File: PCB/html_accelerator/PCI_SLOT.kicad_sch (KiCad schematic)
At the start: 13 parts, among them J2 Bus_PCI_Express_x8, J3 PCIexpress_bracket, U1 MCS9990

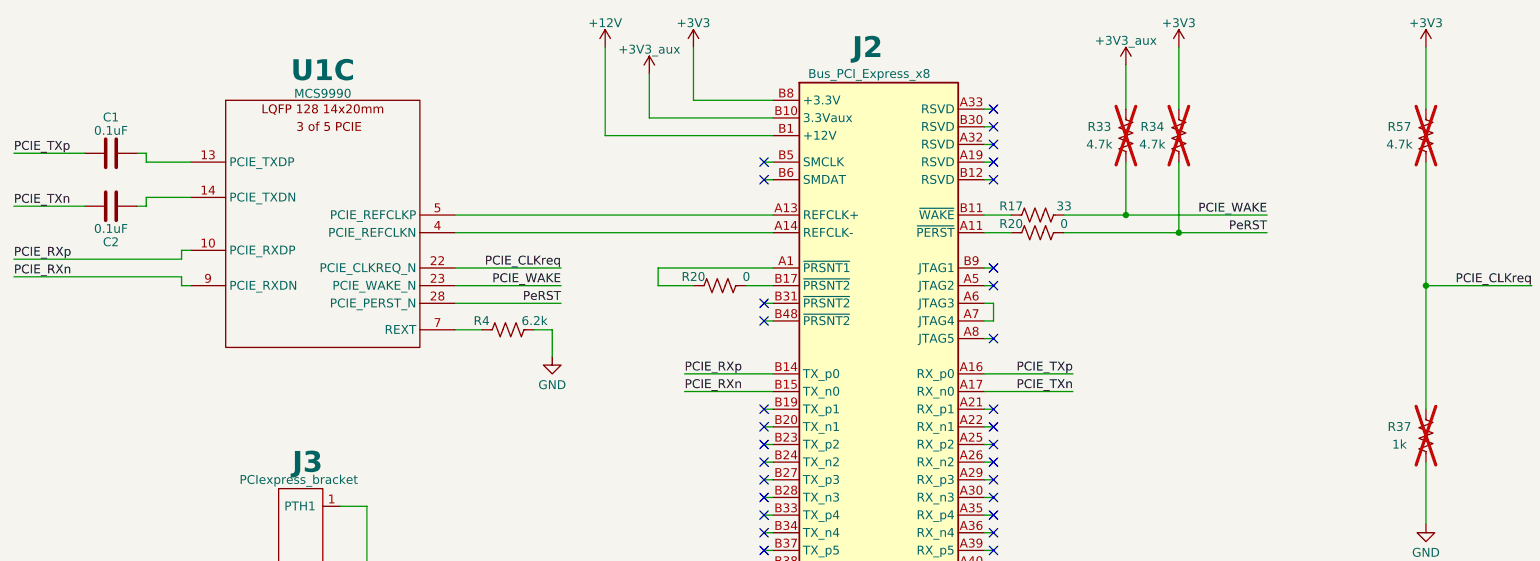
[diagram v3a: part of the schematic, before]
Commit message: EMMC symbols and netlist
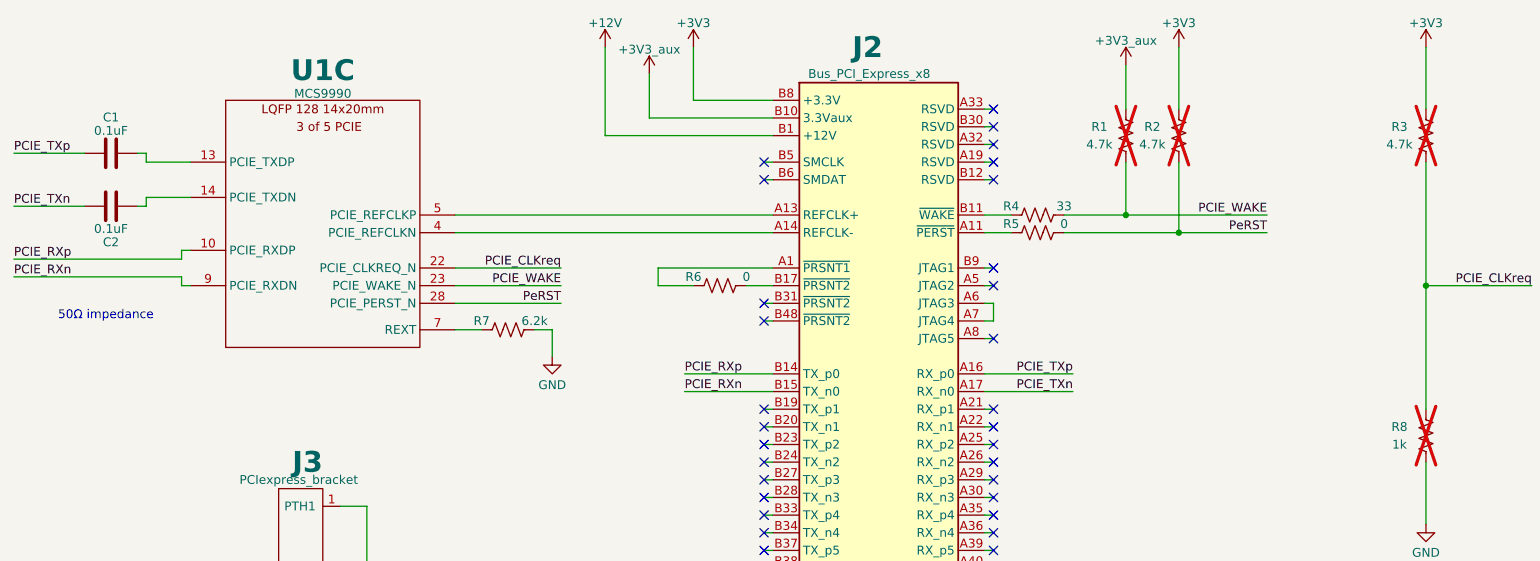
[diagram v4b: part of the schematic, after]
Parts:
- renumbered R33 to R1, R34 to R2, R57 to R3, R17 to R4, R20 to R5, R20 to R6, R4 to R7, R37 to R8
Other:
- note added: "50Ω impedance"
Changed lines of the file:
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@@
     (stroke (width 0) (type default))
+  )
+  (text "50Ω impedance" (at 34.29 95.25 0)
+    (effects (font (size 1.27 1.27)) (justify left bottom))
   )
   (label "PCIE_RXp" (at 124.46 102.87 0) (fields_autoplaced)
@@
   (symbol (lib_id "Device:R_US") (at 129.54 90.17 90) (unit 1)
     (in_bom yes) (on_board yes) (dnp no)
-    (property "Reference" "R20" (at 125.73 88.9 90)
+    (property "Reference" "R6" (at 125.73 88.9 90)
       (effects (font (size 1.27 1.27)))
     )
@@
       (project "html_accelerator"
         (path "/12b3a7c9-141f-40ba-9ebb-094b58bfa6c7/3421334e-11b3-46c8-b0f2-353f0fa6f362"
-          (reference "R20") (unit 1)
+          (reference "R6") (unit 1)
         )
       )
@@
   (symbol (lib_id "power:GND") (at 231.14 124.46 0) (unit 1)
     (in_bom yes) (on_board yes) (dnp no) (fields_autoplaced)
-    (property "Reference" "#PWR010" (at 231.14 130.81 0)
+    (property "Reference" "#PWR08" (at 231.14 130.81 0)
       (effects (font (size 1.27 1.27)) hide)
     )
@@
       (project "html_accelerator"
         (path "/12b3a7c9-141f-40ba-9ebb-094b58bfa6c7/3421334e-11b3-46c8-b0f2-353f0fa6f362"
-          (reference "#PWR010") (unit 1)
+          (reference "#PWR08") (unit 1)
         )
       )
@@
   (symbol (lib_id "power:+3V3") (at 119.38 59.69 0) (unit 1)
     (in_bom yes) (on_board yes) (dnp no)
-    (property "Reference" "#PWR07" (at 119.38 63.5 0)
+    (property "Reference" "#PWR06" (at 119.38 63.5 0)
       (effects (font (size 1.27 1.27)) hide)
     )
@@
       (project "html_accelerator"
         (path "/12b3a7c9-141f-40ba-9ebb-094b58bfa6c7/3421334e-11b3-46c8-b0f2-353f0fa6f362"
-          (reference "#PWR07") (unit 1)
+          (reference "#PWR06") (unit 1)
         )
       )
@@
   (symbol (lib_id "Device:R_US") (at 187.96 68.58 180) (unit 1)
     (in_bom yes) (on_board yes) (dnp yes)
-    (property "Reference" "R33" (at 184.15 67.31 0)
+    (property "Reference" "R1" (at 184.15 67.31 0)
       (effects (font (size 1.27 1.27)))
     )
@@
       (project "html_accelerator"
         (path "/12b3a7c9-141f-40ba-9ebb-094b58bfa6c7/3421334e-11b3-46c8-b0f2-353f0fa6f362"
-          (reference "R33") (unit 1)
+          (reference "R1") (unit 1)
         )
       )
@@
   (symbol (lib_id "power:GND") (at 78.74 140.97 0) (unit 1)
     (in_bom yes) (on_board yes) (dnp no) (fields_autoplaced)
-    (property "Reference" "#PWR01" (at 78.74 147.32 0)
+    (property "Reference" "#PWR09" (at 78.74 147.32 0)
       (effects (font (size 1.27 1.27)) hide)
     )
@@
       (project "html_accelerator"
         (path "/12b3a7c9-141f-40ba-9ebb-094b58bfa6c7/3421334e-11b3-46c8-b0f2-353f0fa6f362"
-          (reference "#PWR01") (unit 1)
+          (reference "#PWR09") (unit 1)
         )
       )
@@
         )
         (path "/12b3a7c9-141f-40ba-9ebb-094b58bfa6c7/3421334e-11b3-46c8-b0f2-353f0fa6f362"
-          (reference "J1") (unit 1)
+          (reference "J2") (unit 1)
         )
       )
@@
   (symbol (lib_id "power:+12V") (at 113.03 55.88 0) (unit 1)
     (in_bom yes) (on_board yes) (dnp no) (fields_autoplaced)
-    (property "Reference" "#PWR04" (at 113.03 59.69 0)
+    (property "Reference" "#PWR01" (at 113.03 59.69 0)
       (effects (font (size 1.27 1.27)) hide)
     )
@@
       (project "html_accelerator"
         (path "/12b3a7c9-141f-40ba-9ebb-094b58bfa6c7/3421334e-11b3-46c8-b0f2-353f0fa6f362"
-          (reference "#PWR04") (unit 1)
+          (reference "#PWR01") (unit 1)
         )
       )
@@
   (symbol (lib_id "power:+3V3") (at 125.73 55.88 0) (unit 1)
     (in_bom yes) (on_board yes) (dnp no) (fields_autoplaced)
-    (property "Reference" "#PWR03" (at 125.73 59.69 0)
+    (property "Reference" "#PWR02" (at 125.73 59.69 0)
       (effects (font (size 1.27 1.27)) hide)
     )
@@
       (project "html_accelerator"
         (path "/12b3a7c9-141f-40ba-9ebb-094b58bfa6c7/3421334e-11b3-46c8-b0f2-353f0fa6f362"
-          (reference "#PWR03") (unit 1)
+          (reference "#PWR02") (unit 1)
         )
       )
@@
   (symbol (lib_id "power:GND") (at 152.4 151.13 0) (unit 1)
     (in_bom yes) (on_board yes) (dnp no) (fields_autoplaced)
-    (property "Reference" "#PWR02" (at 152.4 157.48 0)
+    (property "Reference" "#PWR010" (at 152.4 157.48 0)
       (effects (font (size 1.27 1.27)) hide)
     )
@@
       (project "html_accelerator"
         (path "/12b3a7c9-141f-40ba-9ebb-094b58bfa6c7/3421334e-11b3-46c8-b0f2-353f0fa6f362"
-          (reference "#PWR02") (unit 1)
+          (reference "#PWR010") (unit 1)
         )
       )
@@
   (symbol (lib_id "Device:R_US") (at 99.06 96.52 90) (unit 1)
     (in_bom yes) (on_board yes) (dnp no)
-    (property "Reference" "R4" (at 95.25 95.25 90)
+    (property "Reference" "R7" (at 95.25 95.25 90)
       (effects (font (size 1.27 1.27)))
     )
@@
       (project "html_accelerator"
         (path "/12b3a7c9-141f-40ba-9ebb-094b58bfa6c7/3421334e-11b3-46c8-b0f2-353f0fa6f362"
-          (reference "R4") (unit 1)
+          (reference "R7") (unit 1)
         )
       )
@@
   (symbol (lib_id "Device:R_US") (at 175.26 82.55 90) (unit 1)
     (in_bom yes) (on_board yes) (dnp no)
-    (property "Reference" "R20" (at 171.45 81.28 90)
+    (property "Reference" "R5" (at 171.45 81.28 90)
       (effects (font (size 1.27 1.27)))
     )
@@
       (project "html_accelerator"
         (path "/12b3a7c9-141f-40ba-9ebb-094b58bfa6c7/3421334e-11b3-46c8-b0f2-353f0fa6f362"
-          (reference "R20") (unit 1)
+          (reference "R5") (unit 1)
         )
       )
@@
   (symbol (lib_id "power:+3V3") (at 231.14 55.88 0) (unit 1)
     (in_bom yes) (on_board yes) (dnp no) (fields_autoplaced)
-    (property "Reference" "#PWR09" (at 231.14 59.69 0)
+    (property "Reference" "#PWR04" (at 231.14 59.69 0)
       (effects (font (size 1.27 1.27)) hide)
     )
@@
       (project "html_accelerator"
         (path "/12b3a7c9-141f-40ba-9ebb-094b58bfa6c7/3421334e-11b3-46c8-b0f2-353f0fa6f362"
-          (reference "#PWR09") (unit 1)
+          (reference "#PWR04") (unit 1)
         )
       )
@@
   (symbol (lib_id "Device:R_US") (at 231.14 68.58 180) (unit 1)
     (in_bom yes) (on_board yes) (dnp yes)
-    (property "Reference" "R57" (at 227.33 67.31 0)
+    (property "Reference" "R3" (at 227.33 67.31 0)
       (effects (font (size 1.27 1.27)))
     )
@@
       (project "html_accelerator"
         (path "/12b3a7c9-141f-40ba-9ebb-094b58bfa6c7/3421334e-11b3-46c8-b0f2-353f0fa6f362"
-          (reference "R57") (unit 1)
+          (reference "R3") (unit 1)
         )
       )
@@
   (symbol (lib_id "Device:R_US") (at 175.26 80.01 90) (unit 1)
     (in_bom yes) (on_board yes) (dnp no)
-    (property "Reference" "R17" (at 171.45 78.74 90)
+    (property "Reference" "R4" (at 171.45 78.74 90)
       (effects (font (size 1.27 1.27)))
     )
@@
       (project "html_accelerator"
         (path "/12b3a7c9-141f-40ba-9ebb-094b58bfa6c7/3421334e-11b3-46c8-b0f2-353f0fa6f362"
-          (reference "R17") (unit 1)
+          (reference "R4") (unit 1)
         )
       )
@@
   (symbol (lib_id "power:GND") (at 105.41 100.33 0) (unit 1)
     (in_bom yes) (on_board yes) (dnp no) (fields_autoplaced)
-    (property "Reference" "#PWR05" (at 105.41 106.68 0)
+    (property "Reference" "#PWR07" (at 105.41 106.68 0)
       (effects (font (size 1.27 1.27)) hide)
     )
@@
       (project "html_accelerator"
         (path "/12b3a7c9-141f-40ba-9ebb-094b58bfa6c7/3421334e-11b3-46c8-b0f2-353f0fa6f362"
-          (reference "#PWR05") (unit 1)
+          (reference "#PWR07") (unit 1)
         )
       )
@@
   (symbol (lib_id "Device:R_US") (at 231.14 111.76 180) (unit 1)
     (in_bom yes) (on_board yes) (dnp yes)
-    (property "Reference" "R37" (at 227.33 110.49 0)
+    (property "Reference" "R8" (at 227.33 110.49 0)
       (effects (font (size 1.27 1.27)))
     )
@@
       (project "html_accelerator"
         (path "/12b3a7c9-141f-40ba-9ebb-094b58bfa6c7/3421334e-11b3-46c8-b0f2-353f0fa6f362"
-          (reference "R37") (unit 1)
+          (reference "R8") (unit 1)
         )
       )
@@
   (symbol (lib_id "Device:R_US") (at 195.58 68.58 180) (unit 1)
     (in_bom yes) (on_board yes) (dnp yes)
-    (property "Reference" "R34" (at 191.77 67.31 0)
+    (property "Reference" "R2" (at 191.77 67.31 0)
       (effects (font (size 1.27 1.27)))
     )
@@
       (project "html_accelerator"
         (path "/12b3a7c9-141f-40ba-9ebb-094b58bfa6c7/3421334e-11b3-46c8-b0f2-353f0fa6f362"
-          (reference "R34") (unit 1)
+          (reference "R2") (unit 1)
         )
       )
@@
   (symbol (lib_id "power:+3V3") (at 187.96 58.42 0) (unit 1)
     (in_bom yes) (on_board yes) (dnp no)
-    (property "Reference" "#PWR08" (at 187.96 62.23 0)
+    (property "Reference" "#PWR05" (at 187.96 62.23 0)
       (effects (font (size 1.27 1.27)) hide)
     )
@@
       (project "html_accelerator"
         (path "/12b3a7c9-141f-40ba-9ebb-094b58bfa6c7/3421334e-11b3-46c8-b0f2-353f0fa6f362"
-          (reference "#PWR08") (unit 1)
+          (reference "#PWR05") (unit 1)
         )
       )
@@
   (symbol (lib_id "power:+3V3") (at 195.58 55.88 0) (unit 1)
     (in_bom yes) (on_board yes) (dnp no) (fields_autoplaced)
-    (property "Reference" "#PWR06" (at 195.58 59.69 0)
+    (property "Reference" "#PWR03" (at 195.58 59.69 0)
       (effects (font (size 1.27 1.27)) hide)
     )
@@
       (project "html_accelerator"
         (path "/12b3a7c9-141f-40ba-9ebb-094b58bfa6c7/3421334e-11b3-46c8-b0f2-353f0fa6f362"
-          (reference "#PWR06") (unit 1)
+          (reference "#PWR03") (unit 1)
         )
       )
@@
         )
         (path "/12b3a7c9-141f-40ba-9ebb-094b58bfa6c7/3421334e-11b3-46c8-b0f2-353f0fa6f362"
-          (reference "J2") (unit 1)
+          (reference "J1") (unit 1)
         )
         (path "/12b3a7c9-141f-40ba-9ebb-094b58bfa6c7/c1e0624f-11bc-46dd-864f-01b3a932cae6"

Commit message: 3d part models, PCB netlist imported
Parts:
- C1, C2: footprint (none) -> Capacitor_SMD:C_0805_2012Metric_Pad1.18x1.45mm_HandSolder
- R1, R2, R3, R4, R5, R6, R7, R8: footprint (none) -> Resistor_SMD:R_0805_2012Metric_Pad1.20x1.40mm_HandSolder
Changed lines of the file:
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@@
       (effects (font (size 1.27 1.27)))
     )
-    (property "Footprint" "" (at 129.794 89.154 90)
+    (property "Footprint" "Resistor_SMD:R_0805_2012Metric_Pad1.20x1.40mm_HandSolder" (at 129.794 89.154 90)
       (effects (font (size 1.27 1.27)) hide)
     )
@@
       (effects (font (size 1.27 1.27)))
     )
-    (property "Footprint" "" (at 186.944 68.326 90)
+    (property "Footprint" "Resistor_SMD:R_0805_2012Metric_Pad1.20x1.40mm_HandSolder" (at 186.944 68.326 90)
       (effects (font (size 1.27 1.27)) hide)
     )
@@
       (effects (font (size 1.27 1.27)))
     )
-    (property "Footprint" "" (at 45.72 79.7052 0)
+    (property "Footprint" "Capacitor_SMD:C_0805_2012Metric_Pad1.18x1.45mm_HandSolder" (at 45.72 79.7052 0)
       (effects (font (size 1.27 1.27)) hide)
     )
@@
       (effects (font (size 1.27 1.27)))
     )
-    (property "Footprint" "" (at 99.314 95.504 90)
+    (property "Footprint" "Resistor_SMD:R_0805_2012Metric_Pad1.20x1.40mm_HandSolder" (at 99.314 95.504 90)
       (effects (font (size 1.27 1.27)) hide)
     )
@@
       (effects (font (size 1.27 1.27)))
     )
-    (property "Footprint" "" (at 175.514 81.534 90)
+    (property "Footprint" "Resistor_SMD:R_0805_2012Metric_Pad1.20x1.40mm_HandSolder" (at 175.514 81.534 90)
       (effects (font (size 1.27 1.27)) hide)
     )
@@
       (effects (font (size 1.27 1.27)))
     )
-    (property "Footprint" "" (at 230.124 68.326 90)
+    (property "Footprint" "Resistor_SMD:R_0805_2012Metric_Pad1.20x1.40mm_HandSolder" (at 230.124 68.326 90)
       (effects (font (size 1.27 1.27)) hide)
     )
@@
       (effects (font (size 1.27 1.27)))
     )
-    (property "Footprint" "" (at 175.514 78.994 90)
+    (property "Footprint" "Resistor_SMD:R_0805_2012Metric_Pad1.20x1.40mm_HandSolder" (at 175.514 78.994 90)
       (effects (font (size 1.27 1.27)) hide)
     )
@@
       (effects (font (size 1.27 1.27)))
     )
-    (property "Footprint" "" (at 45.72 70.1548 0)
+    (property "Footprint" "Capacitor_SMD:C_0805_2012Metric_Pad1.18x1.45mm_HandSolder" (at 45.72 70.1548 0)
       (effects (font (size 1.27 1.27)) hide)
     )
@@
       (effects (font (size 1.27 1.27)))
     )
-    (property "Footprint" "" (at 230.124 111.506 90)
+    (property "Footprint" "Resistor_SMD:R_0805_2012Metric_Pad1.20x1.40mm_HandSolder" (at 230.124 111.506 90)
       (effects (font (size 1.27 1.27)) hide)
     )
@@
       (effects (font (size 1.27 1.27)))
     )
-    (property "Footprint" "" (at 194.564 68.326 90)
-      (effects (font (size 1.27 1.27)) hide)
-    )
+    (property "Footprint" "Resistor_SMD:R_0805_2012Metric_Pad1.20x1.40mm_HandSolder" (at 194.564 68.326 90)
+      (effects (font (size 1.27 1.27)) hide)
+    )

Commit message: placement updates
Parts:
- removed J2: Bus_PCI_Express_x8, Connector_PCBEdge:BUS_PCIexpress_x8, symbol Connector:Bus_PCI_Express_x8
- added J1: Bus_PCI_Express_x16, Connector_PCBEdge:BUS_PCIexpress_x16, symbol Connector:Bus_PCI_Express_x16
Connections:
- net +12V: now also J1.A2 (+12V), J1.A3 (+12V), J1.B1 (+12V), J1.B2 (+12V), J1.B3 (+12V)
- net +3V3: now also J1.A10 (+3.3V), J1.A9 (+3.3V), J1.B8 (+3.3V); no longer R1.2
- net GND: now also J1.A12 (GND), J1.A15 (GND), J1.A18 (GND), J1.A20 (GND), J1.A23 (GND), J1.A24 (GND), J1.A27 (GND), J1.A28 (GND), J1.A31 (GND), J1.A34 (GND), J1.A37 (GND), J1.A38 (GND), J1.A4 (GND), J1.A41 (GND), J1.A42 (GND), J1.A45 (GND), J1.A46 (GND), J1.A49 (GND), J1.A51 (GND), J1.A54 (GND), J1.A55 (GND), J1.A58 (GND), J1.A59 (GND), J1.A62 (GND), J1.A63 (GND), J1.A66 (GND), J1.A67 (GND), J1.A70 (GND), J1.A71 (GND), J1.A74 (GND), J1.A75 (GND), J1.A78 (GND), J1.A79 (GND), J1.A82 (GND), J1.B13 (GND), J1.B16 (GND), J1.B18 (GND), J1.B21 (GND), J1.B22 (GND), J1.B25 (GND), J1.B26 (GND), J1.B29 (GND), J1.B32 (GND), J1.B35 (GND), J1.B36 (GND), J1.B39 (GND), J1.B4 (GND), J1.B40 (GND), J1.B43 (GND), J1.B44 (GND), J1.B47 (GND), J1.B49 (GND), J1.B52 (GND), J1.B53 (GND), J1.B56 (GND), J1.B57 (GND), J1.B60 (GND), J1.B61 (GND), J1.B64 (GND), J1.B65 (GND), J1.B68 (GND), J1.B69 (GND), J1.B7 (GND), J1.B72 (GND), J1.B73 (GND), J1.B76 (GND), J1.B77 (GND), J1.B80 (GND)
- net PCIE_RXn: now also J1.B15 (PETn0)
- net PCIE_RXp: now also J1.B14 (PETp0)
- net PCIE_TXn: now also J1.A17 (PERn0)
- net PCIE_TXp: now also J1.A16 (PERp0)
- net at R6.1: now also J1.A1 (~{PRSNT1})
- net at R6.2: now also J1.B17 (~{PRSNT2})
- net at R5.1: now also J1.A11 (~{PERST})
- net at R4.1: now also J1.B11 (~{WAKE})
- net at U1.4 (PCIE_REFCLKN): now also J1.A14 (REFCLK-)
- net at U1.5 (PCIE_REFCLKP): now also J1.A13 (REFCLK+)
- new net: J1.A6 (JTAG3), J1.A7 (JTAG4)
- new net +3V0: J1.B10 (3.3Vaux), R1.2
- no-connect marks 40 -> 75
